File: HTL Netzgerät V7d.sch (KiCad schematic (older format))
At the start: 56 parts, among them T1 BC547, T2 BC547, T3 BC547, T4 BC547, T5 BC547, T6 BC557, T7 BC557, T8 BC639, T9 -NPN-TO3, X1 PINHD-1X1, X10 PINHD-1X1, X11 PINHD-1X1, X12 PINHD-1X1, X13 PINHD-1X1, X14 PINHD-1X1, X15 PINHD-1X1, X2 PINHD-1X1, X3 PINHD-1X1, X4 PINHD-1X1, X5 PINHD-1X1, X6 PINHD-1X1, X7 PINHD-1X1, X8 PINHD-1X1, X9 PINHD-1X1

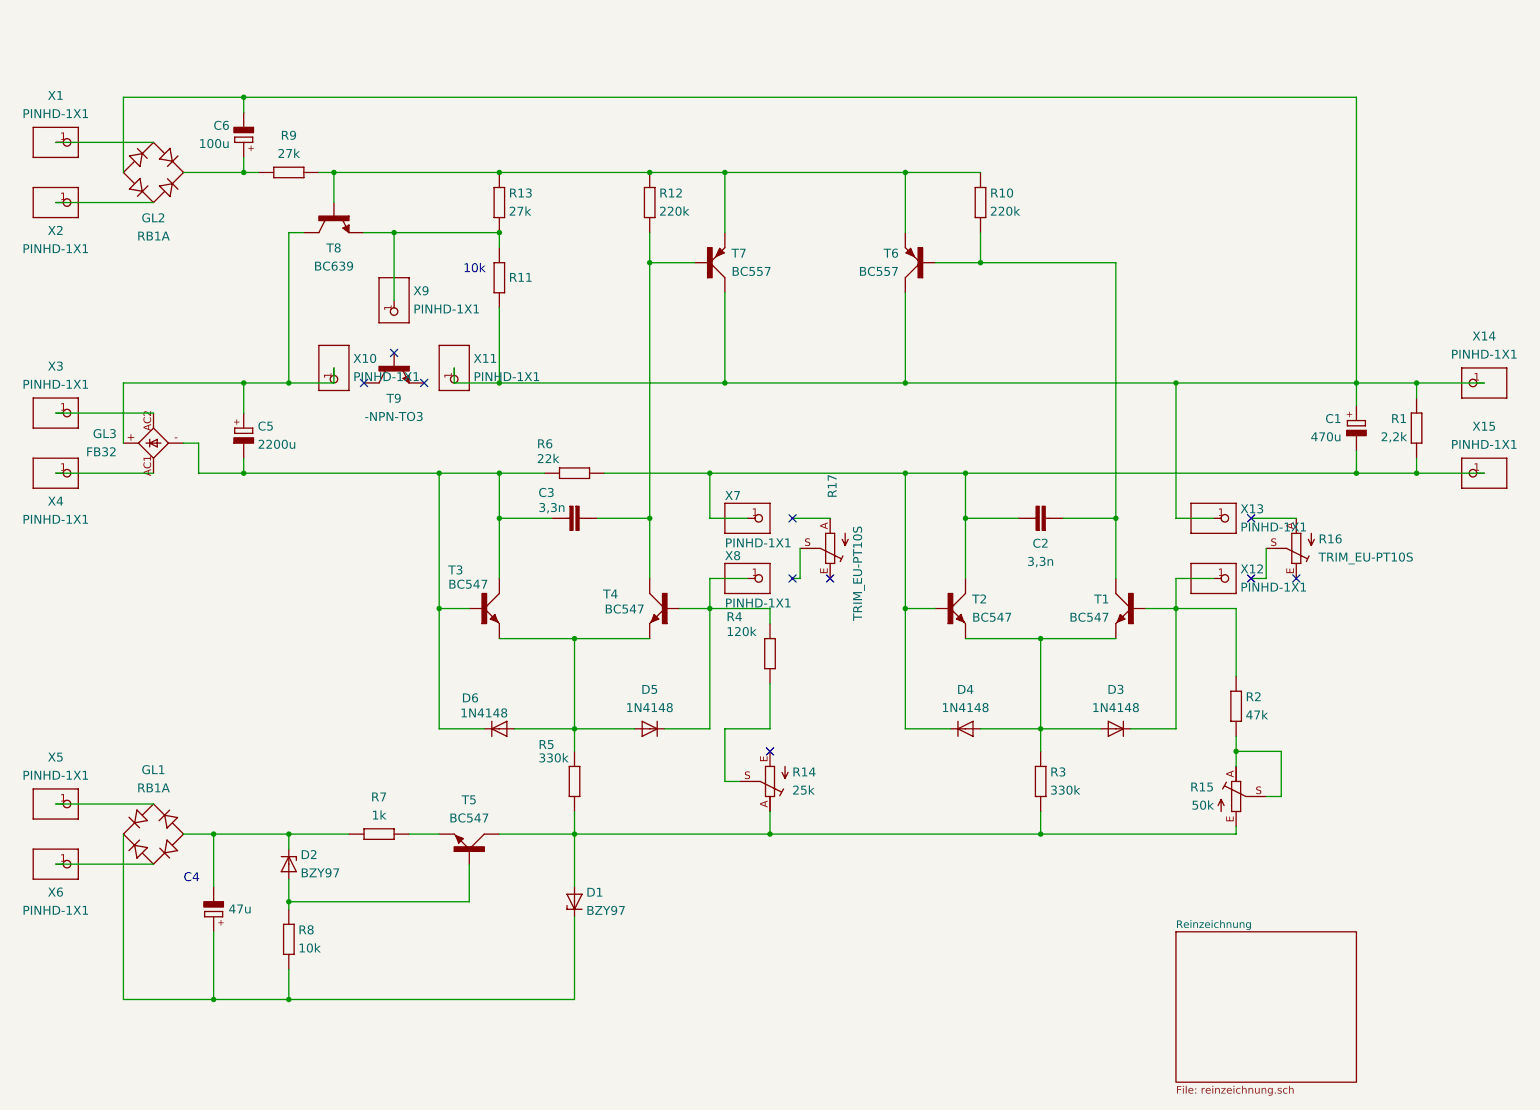
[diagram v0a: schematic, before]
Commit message: Reinzeichnung ins Hauptdokument verschoben, Hauptdokument gelöscht
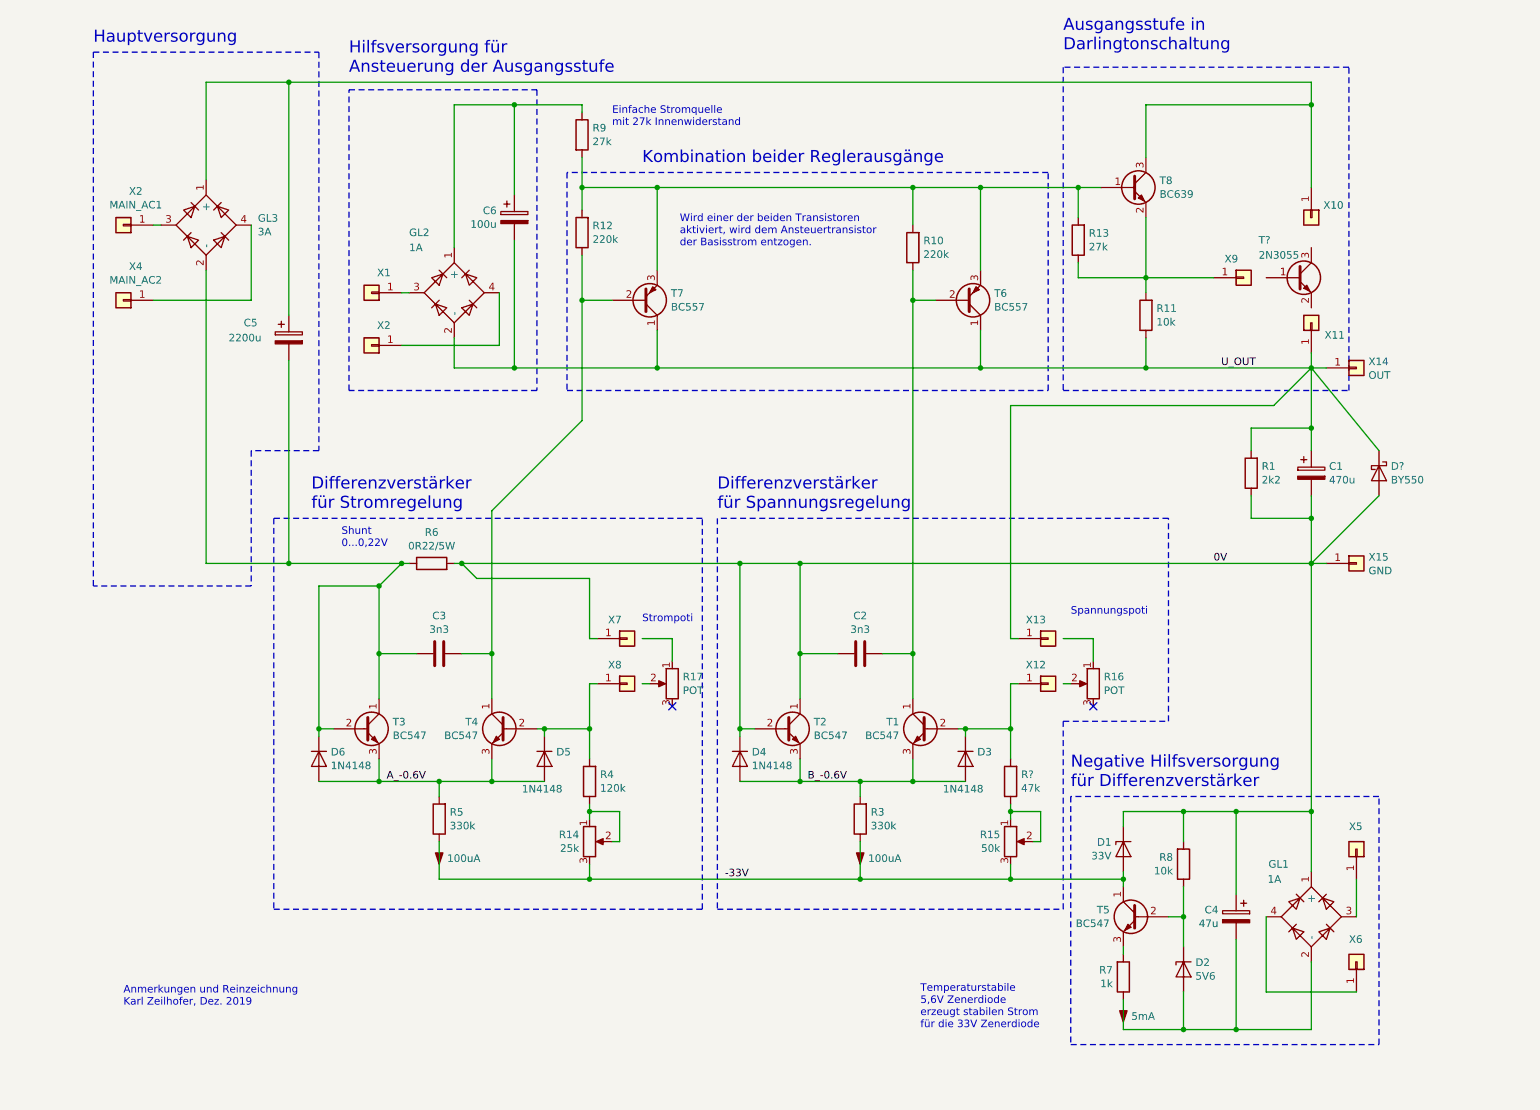
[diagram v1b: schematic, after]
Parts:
- removed C1: 470u, HTL Netzgerät V7d:E5-13, symbol HTL_Netzgerät_V7d-eagle-import:CPOL-EUE5-13
- removed C2, C3: 3,3n, HTL Netzgerät V7d:C050-050X075, symbol HTL_Netzgerät_V7d-eagle-import:C-EU050-050X075
- removed C4: 47u, HTL Netzgerät V7d:E5-8,5, symbol HTL_Netzgerät_V7d-eagle-import:CPOL-EUE5-8.5
- removed C5: 2200u, HTL Netzgerät V7d:E35-18, symbol HTL_Netzgerät_V7d-eagle-import:CPOL-EUE35-18AXIAL
- removed C6: 100u, HTL Netzgerät V7d:E5-8,5, symbol HTL_Netzgerät_V7d-eagle-import:CPOL-EUE5-8.5
- removed D1, D2: BZY97, HTL Netzgerät V7d:F126Z12, symbol HTL_Netzgerät_V7d-eagle-import:BZY97
- removed D3, D4, D5, D6: 1N4148, HTL Netzgerät V7d:DO35-10, symbol HTL_Netzgerät_V7d-eagle-import:1N4148
- removed GL1, GL2: RB1A, HTL Netzgerät V7d:RB1A, symbol HTL_Netzgerät_V7d-eagle-import:RB1A
- removed GL3: FB32, HTL Netzgerät V7d:FB32, symbol HTL_Netzgerät_V7d-eagle-import:FB32
- removed R1: 2,2k, HTL Netzgerät V7d:0207_12, symbol HTL_Netzgerät_V7d-eagle-import:R-EU_0207_12
- removed R10, R12: 220k, HTL Netzgerät V7d:0207_12, symbol HTL_Netzgerät_V7d-eagle-import:R-EU_0207_12
- removed R11, R8: 10k, HTL Netzgerät V7d:0207_12, symbol HTL_Netzgerät_V7d-eagle-import:R-EU_0207_12
- removed R13, R9: 27k, HTL Netzgerät V7d:0207_12, symbol HTL_Netzgerät_V7d-eagle-import:R-EU_0207_12
- removed R14: 25k, HTL Netzgerät V7d:LI15, symbol HTL_Netzgerät_V7d-eagle-import:R-TRIMM15
- removed R15: 50k, HTL Netzgerät V7d:LI15, symbol HTL_Netzgerät_V7d-eagle-import:R-TRIMM15
- removed R16, R17: TRIM_EU-PT10S, HTL Netzgerät V7d:PT-10S, symbol HTL_Netzgerät_V7d-eagle-import:TRIM_EU-PT10S
- removed R2: 47k, HTL Netzgerät V7d:0207_12, symbol HTL_Netzgerät_V7d-eagle-import:R-EU_0207_12
- removed R3, R5: 330k, HTL Netzgerät V7d:0207_12, symbol HTL_Netzgerät_V7d-eagle-import:R-EU_0207_12
- removed R4: 120k, HTL Netzgerät V7d:0207_12, symbol HTL_Netzgerät_V7d-eagle-import:R-EU_0207_12
- removed R6: 22k, HTL Netzgerät V7d:0617_22, symbol HTL_Netzgerät_V7d-eagle-import:R-EU_0617_22
- removed R7: 1k, HTL Netzgerät V7d:0207_12, symbol HTL_Netzgerät_V7d-eagle-import:R-EU_0207_12
- removed T1, T2, T3, T4, T5: BC547, HTL Netzgerät V7d:TO92, symbol HTL_Netzgerät_V7d-eagle-import:BC547_HTL
- removed T6, T7: BC557, HTL Netzgerät V7d:TO92, symbol HTL_Netzgerät_V7d-eagle-import:BC557_HTL
- removed T8: BC639, HTL Netzgerät V7d:TO92-BCE, symbol HTL_Netzgerät_V7d-eagle-import:-NPN-TO92-BCE
- removed T9: -NPN-TO3, HTL Netzgerät V7d:TO3, symbol HTL_Netzgerät_V7d-eagle-import:-NPN-TO3
- removed X1, X10, X11, X12, X13, X14, X15, X2, X3, X4, X5, X6, X7, X8, X9: PINHD-1X1, HTL Netzgerät V7d:1X01, symbol HTL_Netzgerät_V7d-eagle-import:PINHD-1X1
- added C1: 470u, symbol v5_Device:CP
- added C2, C3: 3n3, symbol v5_Device:C
- added C4: 47u, symbol v5_Device:CP
- added C5: 2200u, symbol v5_Device:CP
- added C6: 100u, symbol v5_Device:CP
- added D1: 33V, symbol v5_Device:D_Zener
- added D2: 5V6, symbol v5_Device:D_Zener
- added D3, D4, D5, D6: 1N4148, symbol v5_Device:D
- added D?: BY550, symbol v5_Device:D_Schottky
- added GL1, GL2: 1A, symbol v4_device:D_Bridge_+-AA
- added GL3: 3A, symbol v4_device:D_Bridge_+-AA
- added I? (x2): 100uA, symbol t14_testing:Current
- added I?: 5mA, symbol t14_testing:Current
- added R1: 2k2, symbol v5_Device:R
- added R10, R12: 220k, symbol v5_Device:R
- added R11, R8: 10k, symbol v5_Device:R
- added R13, R9: 27k, symbol v5_Device:R
- added R14: 25k, symbol v5_Device:R_POT
- added R15: 50k, symbol v5_Device:R_POT
- added R16, R17: POT, symbol v5_Device:R_POT
- added R3, R5: 330k, symbol v5_Device:R
- added R4: 120k, symbol v5_Device:R
- added R6: 0R22/5W, symbol v5_Device:R
- added R7: 1k, symbol v5_Device:R
- added R?: 47k, symbol v5_Device:R
- added T1, T2, T3, T4, T5: BC547, TO_SOT_Packages_THT:TO-92_Molded_Narrow, symbol v4_Transistor:BC547
- added T6, T7: BC557, Package_TO_SOT_THT:TO-92_Inline, symbol v5_Transistor_BJT:BC557
- added T8: BC639, symbol v5_Device:Q_NPN_BEC
- added T?: 2N3055, symbol v5_Device:Q_NPN_BEC
- added X1: AUX1_AC1, symbol v4_Connector:Conn_01x01
- added X10: C, symbol v4_Connector:Conn_01x01
- added X11: E, symbol v4_Connector:Conn_01x01
- added X12: VPOT-, symbol v4_Connector:Conn_01x01
- added X13: VPOT+, symbol v4_Connector:Conn_01x01
- added X14: OUT, symbol v4_Connector:Conn_01x01
- added X15: GND, symbol v4_Connector:Conn_01x01
- added X2: AUX1_AC2, symbol v4_Connector:Conn_01x01
- added X2: MAIN_AC1, symbol v4_Connector:Conn_01x01
- added X4: MAIN_AC2, symbol v4_Connector:Conn_01x01
- added X5: AUX2_AC1, symbol v4_Connector:Conn_01x01
- added X6: AUX2_AC2, symbol v4_Connector:Conn_01x01
- added X7: IPOT+, symbol v4_Connector:Conn_01x01
- added X8: IPOT-, symbol v4_Connector:Conn_01x01
- added X9: B, symbol v4_Connector:Conn_01x01
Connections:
- new net: C6.1, GL2.1 (+), R9.1
- new net: GL2.3, X1.1 (Pin_1)
- new net: GL2.4, X2.1 (Pin_1)
- new net: R10.2, R12.2, R13.2, R9.2, T6.3 (E), T7.3 (E), T8.1 (B)
- new net: R11.2, R13.1, T8.2 (E), X9.1 (Pin_1)
- new net: C5.1, GL3.1 (+), T8.3 (C), X10.1 (Pin_1)
- new net: C3.2, C5.2, D6.1 (K), GL3.2 (-), R6.1, T3.1 (C), T3.2 (B)
- new net: GL3.3, X2.1 (Pin_1)
- new net: GL3.4, X4.1 (Pin_1)
- new net: C3.1, R12.1, T4.1 (C), T7.2 (B)
- new net: C2.1, R10.1, T1.1 (C), T6.2 (B)
- new net: C4.2, D2.2 (A), GL1.2 (-), R7.1
- new net: GL1.3, X5.1 (Pin_1)
- new net: GL1.4, X6.1 (Pin_1)
- new net: D2.1 (K), R8.1, T5.2 (B)
- new net: R7.2, T5.3 (E)
- new net: D3.1 (K), R?.2, T1.2 (B), X12.1 (Pin_1)
- new net: R15.1, R15.2, R?.1
- new net: D5.1 (K), R4.2, T4.2 (B), X8.1 (Pin_1)
- new net: R14.1, R14.2, R4.1
- new net -33V: D1.2 (A), R14.3, R15.3, R3.1, R5.1, T5.1 (C)
- new net 0V: C1.2, C2.2, C4.1, D1.1 (K), D4.1 (K), D?.2 (A), GL1.1 (+), R1.1, R6.2, R8.2, T2.1 (C), T2.2 (B), X15.1 (Pin_1), X7.1 (Pin_1)
- new net A_-0.6V: D5.2 (A), D6.2 (A), R5.2, T3.3 (E), T4.3 (E)
- new net B_-0.6V: D3.2 (A), D4.2 (A), R3.2, T1.3 (E), T2.3 (E)
- new net U_OUT: C1.1, C6.2, D?.1 (K), GL2.2 (-), R1.2, R11.1, T6.1 (C), T7.1 (C), X11.1 (Pin_1), X13.1 (Pin_1), X14.1 (Pin_1)
- no-connect marks 10 -> 2
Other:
- note added: "Anmerkungen und Reinzeichnung\nKarl Zeilhofer, Dez. 2019"
- note added: "Ausgangsstufe in\nDarlingtonschaltung"
- note added: "Differenzverstärker\nfür Spannungsregelung"
- note added: "Differenzverstärker\nfür Stromregelung"
- note added: "Einfache Stromquelle\nmit 27k Innenwiderstand"
- note added: "Hauptversorgung"
- note added: "Hilfsversorgung für \nAnsteuerung der Ausgangsstufe"
- note added: "Kombination beider Reglerausgänge"
- note added: "Negative Hilfsversorgung \nfür Differenzverstärker"
- note added: "Shunt\n0...0,22V"
- note added: "Spannungspoti"
- note added: "Strompoti"
- note added: "Temperaturstabile \n5,6V Zenerdiode\nerzeugt stabilen Strom\nfür die 33V Zenerdiode"
- note added: "Wird einer der beiden Transistoren \naktiviert, wird dem Ansteuertransistor\nder Basisstrom entzogen."
- note removed: "10k"
- note removed: "C4"

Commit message: neue footprints zugeordnet im Schaltplan
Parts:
- C1: footprint (none) -> v5_Capacitor_THT:CP_Radial_D13.0mm_P5.00mm
- C2, C3: footprint (none) -> v5_Capacitor_THT:C_Rect_L7.2mm_W4.5mm_P5.00mm_FKS2_FKP2_MKS2_MKP2
- C4, C6: footprint (none) -> v5_Capacitor_THT:CP_Radial_D8.0mm_P5.00mm
- C5: footprint (none) -> v5_Capacitor_THT:CP_Axial_L30.0mm_D18.0mm_P35.00mm_Horizontal
- D1, D2, D3, D4, D5, D6: footprint (none) -> v5_Diode_THT:D_A-405_P12.70mm_Horizontal
- D_Ext1: renamed from D?; footprint (none) -> v5_Diode_THT:D_DO-27_P15.24mm_Horizontal
- GL1, GL2: footprint (none) -> v5_Diode_THT:Diode_Bridge_Round_D9.0mm
- GL3: footprint (none) -> v5_Diode_THT:Diode_Bridge_32.0x5.6x17.0mm_P10.0mm_P7.5mm
- R1, R10, R11, R12, R13, R14, R15, R16, R17, R3, R4, R5, R6, R7, R8, R9: footprint (none) -> v5_Resistor_THT:R_Axial_DIN0411_L9.9mm_D3.6mm_P12.70mm_Horizontal
- R2: renamed from R?; footprint (none) -> v5_Resistor_THT:R_Axial_DIN0411_L9.9mm_D3.6mm_P12.70mm_Horizontal
- T1, T2, T3, T4, T5: footprint TO_SOT_Packages_THT:TO-92_Molded_Narrow -> v5_Package_TO_SOT_THT:TO-92_Inline
- T6, T7: footprint Package_TO_SOT_THT:TO-92_Inline -> v5_Package_TO_SOT_THT:TO-92_Inline
- T8: footprint (none) -> v5_Package_TO_SOT_THT:TO-92_Inline
- T_Ext1: renamed from T?; footprint (none) -> v5_Package_TO_SOT_THT:TO-3
- X1, X10, X11, X12, X13, X14, X15, X2, X4, X5, X6, X7, X8, X9: footprint (none) -> v5_TestPoint:TestPoint_THTPad_D2.5mm_Drill1.2mm
- X3: renamed from X2; footprint (none) -> v5_TestPoint:TestPoint_THTPad_D2.5mm_Drill1.2mm
- gave numbers to parts that had none: 3
